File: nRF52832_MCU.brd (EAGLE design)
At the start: 37.5 x 22.2 mm, 31 parts, among them J100 DEBUG_CONNECTOR, P1 WIREPADSMD1,27-254, P2 WIREPADSMD1,27-254, P3 WIREPADSMD1,27-254, P4 WIREPADSMD1,27-254, U1 NRF52832, X1 32MHz, X2 32.768kHz

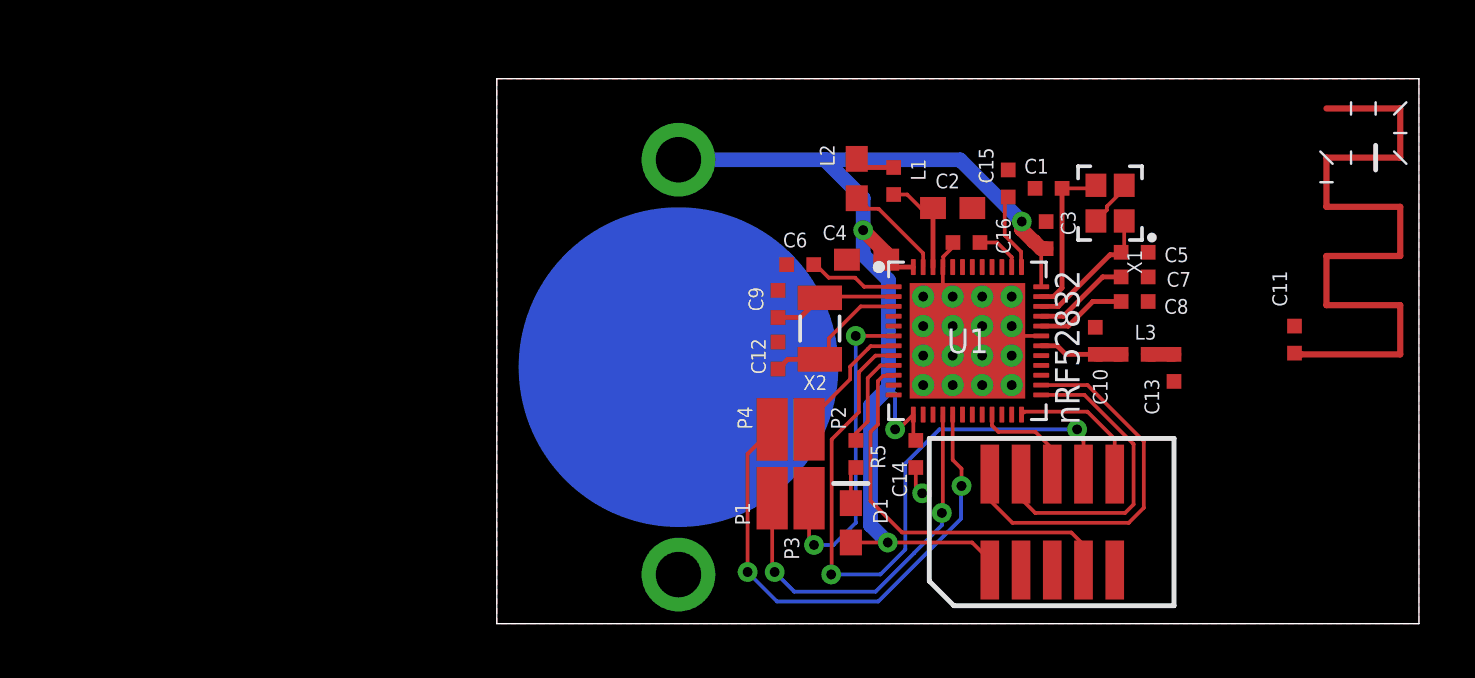
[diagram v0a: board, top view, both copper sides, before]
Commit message: Antenna airwire without detour
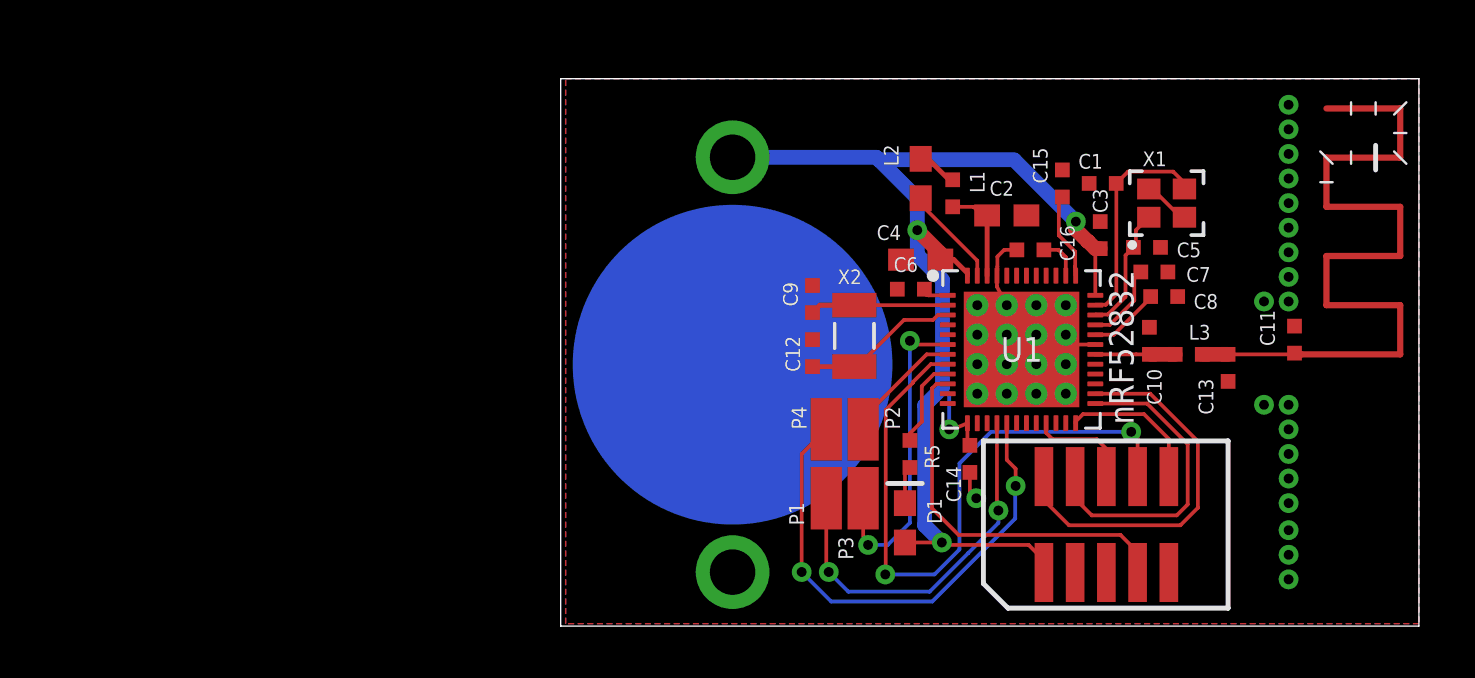
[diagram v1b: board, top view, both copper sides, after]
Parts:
- moved C6 4.61 mm to (35.0, 13.5)
- moved C16 2.62 mm to (39.9, 15.1)
- moved L2 2.60 mm to (35.4, 18.0)
- moved L1 2.45 mm to (36.7, 17.4)
- moved X1 2.30 mm to (45.4, 17.0), turned to 0 degrees
- moved U1 2.23 mm to (39.5, 11.1)
- moved C2 2.22 mm to (38.9, 16.5)
- moved C1 2.21 mm to (42.8, 17.8)
- moved C14 2.21 mm to (37.4, 6.60)
- moved J100 2.20 mm to (43.0, 3.93)
- moved BATT1 2.20 mm to (27.8, 10.4)
- moved C10 2.20 mm to (44.7, 11.4)
- moved C15 2.20 mm to (41.2, 17.8)
- moved C3 2.20 mm to (42.7, 15.7)
- moved L3 2.20 mm to (46.3, 10.8)
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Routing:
- net N$5: track 1.37 -> 4.37 mm
- net N$3: track 6.47 -> 8.96 mm
- net DEC1: track 3.62 -> 1.35 mm
- net GND: track 8.03 -> 9.07 mm
- net DEC2: track 3.66 -> 2.92 mm
- net DEC3: track 3.91 -> 3.26 mm
- net P0.08_RX: track 16.2 -> 15.5 mm
- net XL1: track 5.05 -> 5.62 mm
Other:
- board size 37.5 x 22.2 mm -> 34.9 x 22.3 mm

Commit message: Update dec capacitor orrientation
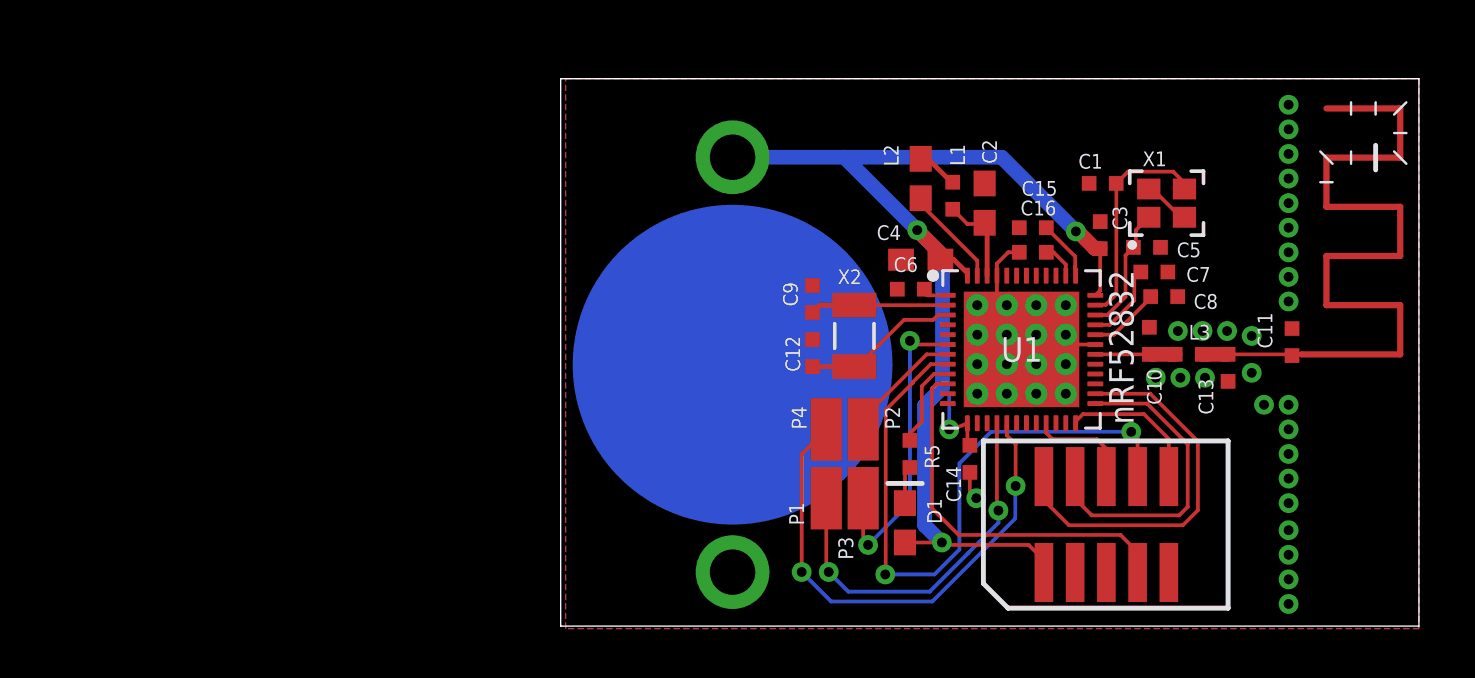
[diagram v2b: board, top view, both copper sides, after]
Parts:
- moved C15 2.16 mm to (40.0, 16.0), turned to 180 degrees
- moved C2 1.03 mm to (38.0, 17.0), turned to 90 degrees
- moved C11 0.14 mm to (50.5, 11.3)
- moved C16 0.14 mm to (40.0, 15.0)
- moved L1 0.10 mm to (36.7, 17.3)
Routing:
- net P0.25: track 3.53 -> 2.44 mm

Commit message: Update labels and restrict masks
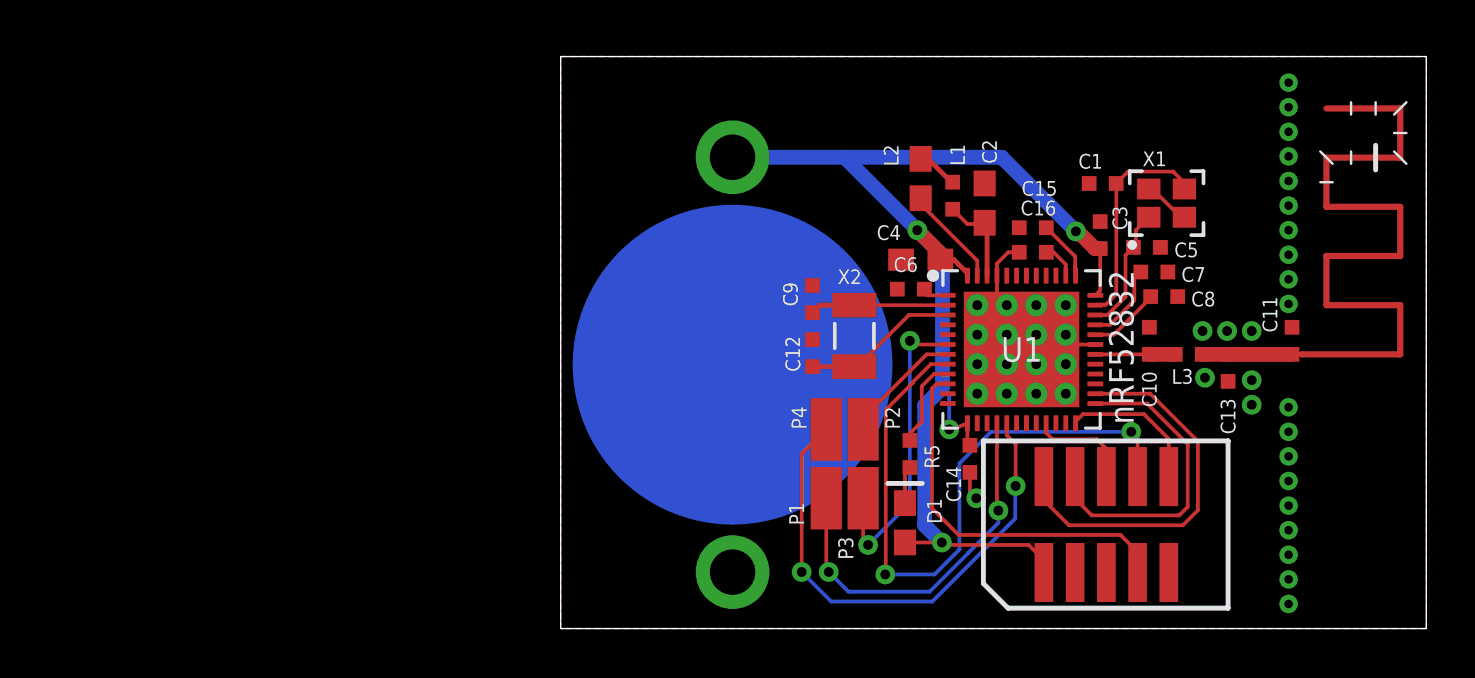
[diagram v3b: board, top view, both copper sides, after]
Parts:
- moved C11 0.05 mm to (50.5, 11.4)
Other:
- board size 34.9 x 22.3 mm -> 35.2 x 23.3 mm

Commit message: Remove DRC errors
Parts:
- moved R5 20.8 mm to (14.2, 8.10)
- moved C9 20.8 mm to (10.2, 13.6)
- moved C1 20.8 mm to (22.0, 18.1)
- moved C8 20.8 mm to (24.5, 13.5)
- moved L1 20.8 mm to (15.9, 17.6)
- moved L3 20.8 mm to (25.5, 11.2)
- moved C10 20.8 mm to (23.9, 11.7)
- moved C11 20.8 mm to (29.7, 11.7)
- moved C15 20.8 mm to (19.2, 16.3)
- moved C16 20.8 mm to (19.2, 15.3)
- moved C2 20.8 mm to (17.2, 17.3)
- moved C3 20.8 mm to (21.9, 16.0)
- moved C5 20.8 mm to (23.8, 15.5)
- moved J100 20.8 mm to (22.2, 4.23)
- moved P1 20.8 mm to (10.8, 5.30)
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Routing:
- net VDD_P3V3: track 49.4 -> 45.5 mm
- net P0.06_TX: track 26.4 -> 23.7 mm
- net P0.13: track 15.5 -> 14.2 mm
- net P0.14: track 20.8 -> 19.8 mm
- net P0.07: track 3.67 -> 2.67 mm

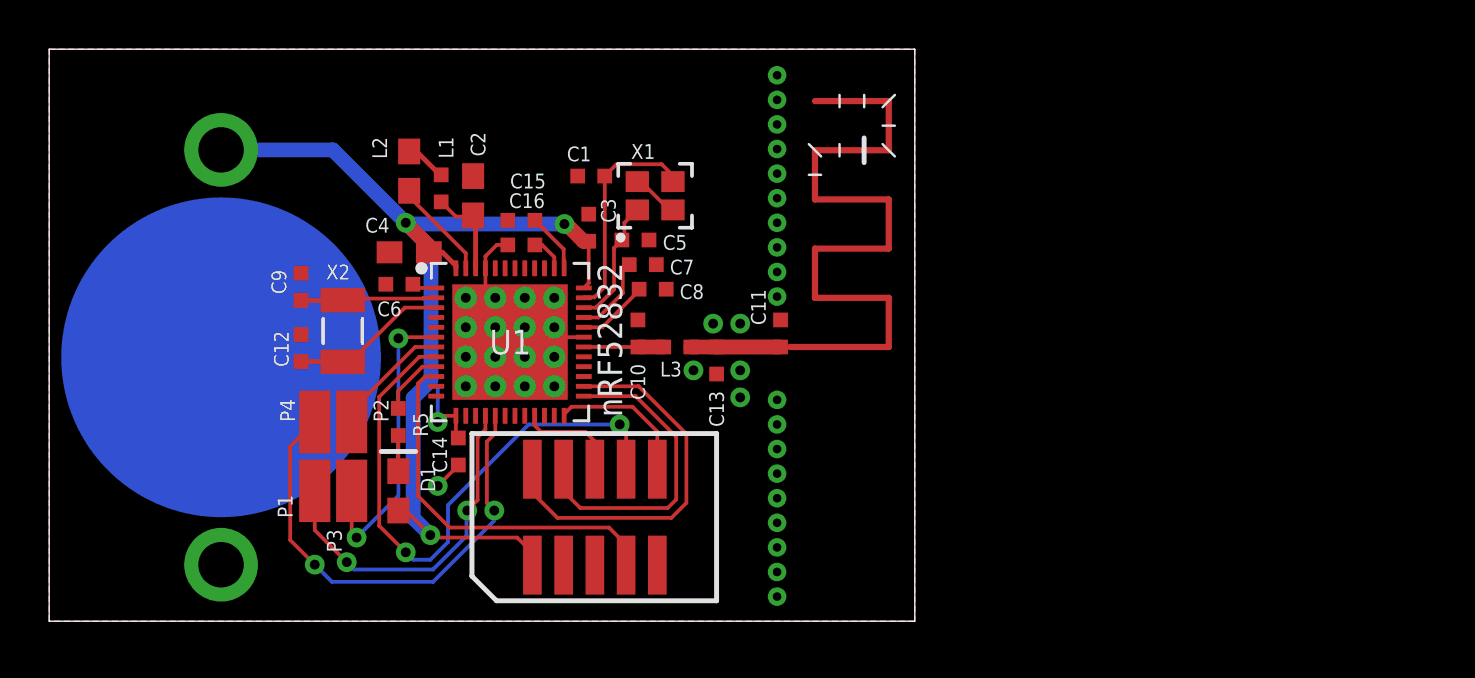
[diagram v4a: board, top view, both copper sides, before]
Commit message: Add board version
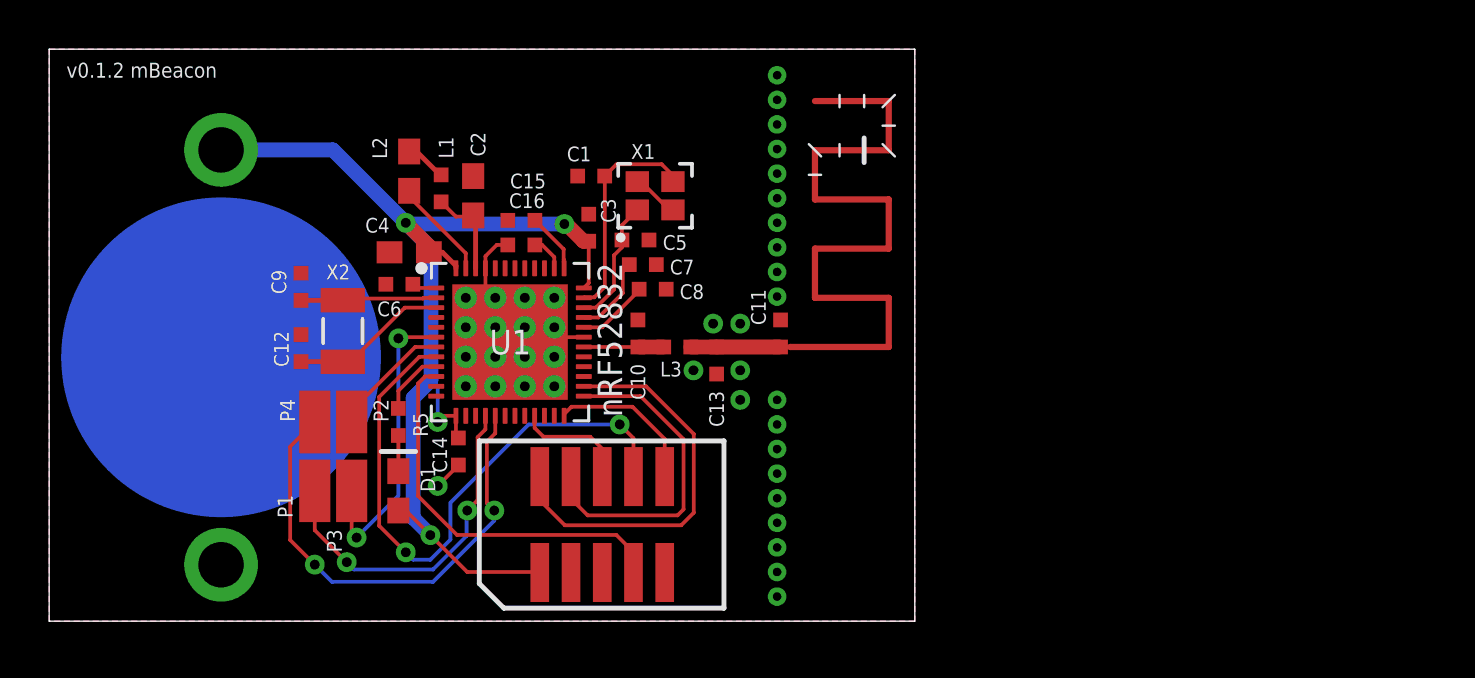
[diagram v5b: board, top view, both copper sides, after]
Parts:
- moved J100 0.42 mm to (22.5, 3.93)
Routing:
- net SWDIO: track 15.7 -> 16.6 mm
- net SWDCLK: track 13.0 -> 13.5 mm
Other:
- board text added: "v0.1.2 mBeacon"
